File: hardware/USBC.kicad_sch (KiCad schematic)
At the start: 16 parts, among them J20 USB_C_Receptacle_USB2.0_16P, U11 CDSOT236-0504C, U33 USBLC6-2P6, U8 CP2102N-A02-GQFN20

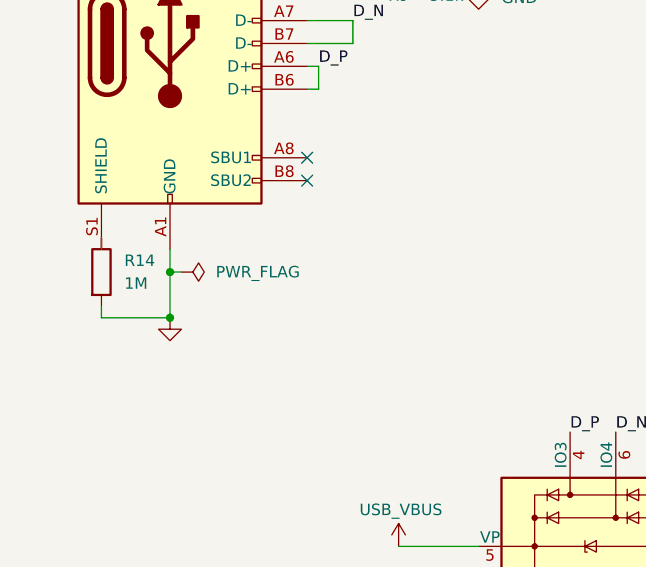
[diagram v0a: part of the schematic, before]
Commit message: passing ERC w/ exclusions
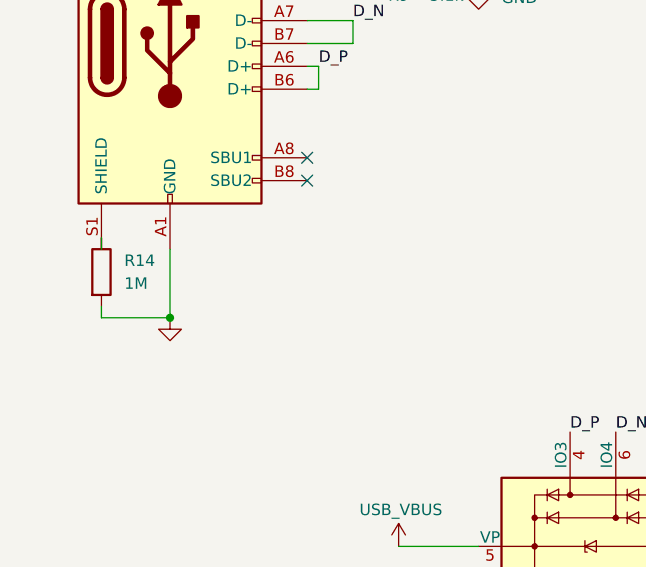
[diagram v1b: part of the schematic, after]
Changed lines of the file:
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@@
-	)
-	(junction
-		(at 55.88 105.41)
-		(diameter 0)
-		(color 0 0 0 0)
 	)
 	(junction
@@
 	(wire
 		(pts
-			(xy 55.88 110.49) (xy 55.88 105.41)
-		)
-		(stroke
-			(width 0)
-			(type default)
-		)
-	)
-	(wire
-		(pts
 			(xy 72.39 82.55) (xy 72.39 85.09)
 		)
@@
 	(wire
 		(pts
-			(xy 55.88 105.41) (xy 55.88 102.87)
+			(xy 55.88 102.87) (xy 55.88 110.49)
 		)
 		(stroke
@@
 		(pts
 			(xy 246.38 100.33) (xy 250.19 100.33)
-		)
-		(stroke
-			(width 0)
-			(type default)
-		)
-	)
-	(wire
-		(pts
-			(xy 55.88 105.41) (xy 57.15 105.41)
 		)
 		(stroke
@@
 					(unit 1)
 				)
-			)
-		)
-	)
-	(symbol
-		(lib_id "power:PWR_FLAG")
-		(at 57.15 105.41 270)
-		(unit 1)
-		(exclude_from_sim no)
-		(in_bom yes)
-		(on_board yes)
-		(dnp no)
-		(fields_autoplaced yes)
-		(property "Reference" "#FLG0108"
-			(at 59.055 105.41 0)
-			(effects
-				(font
-					(size 1.27 1.27)
-				)
-				(hide yes)
-			)
-		)
-		(property "Value" "PWR_FLAG"
-			(at 60.96 105.4099 90)
-			(effects
-				(font
-					(size 1.27 1.27)
-				)
-				(justify left)
-			)
-		)
-		(property "Footprint" ""
-			(at 57.15 105.41 0)
-			(effects
-				(font
-					(size 1.27 1.27)
-				)
-				(hide yes)
-			)
-		)
-		(property "Datasheet" "~"
-			(at 57.15 105.41 0)
-			(effects
-				(font
-					(size 1.27 1.27)
-				)
-				(hide yes)
-			)
-		)
-		(property "Description" "Special symbol for telling ERC where power comes from"
-			(at 57.15 105.41 0)
-			(effects
-				(font
-					(size 1.27 1.27)
-				)
-				(hide yes)
-			)
-		)
-		(pin "1"
-		)
-		(instances
-			(project "Senior_Design"
-				(path "/8f5928e8-0fc1-4443-a20f-3bfeb956761e/53a20cc4-87c9-41e2-9c0c-c30bc75df497"
-					(reference "#FLG0108")
-					(unit 1)
-				)

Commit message: updated annotations
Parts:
- renumbered C90 to C601, C14 to C602, D13 to D601, D14 to D602, J20 to J601, R14 to R601, R300 to R602, R9 to R603, R27 to R604, R28 to R605, R24 to R606, R25 to R607, R26 to R608, U11 to U601, U33 to U602, U8 to U603

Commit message: wip
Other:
- moved on the sheet: C601, C602, D601, D602, J601, R601, R602, R603, R604, R605, R606, R607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

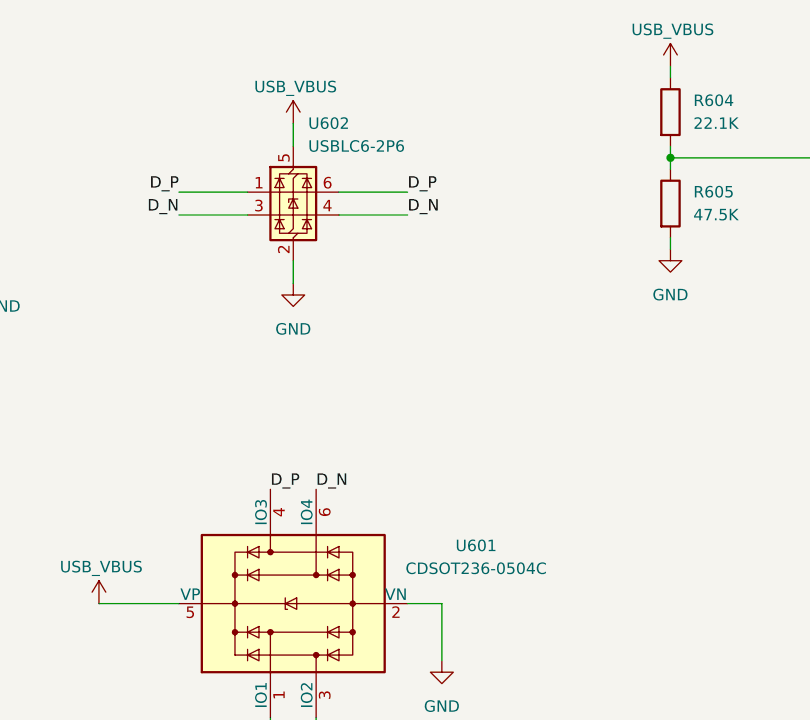
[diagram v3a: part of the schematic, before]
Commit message: added ship fet
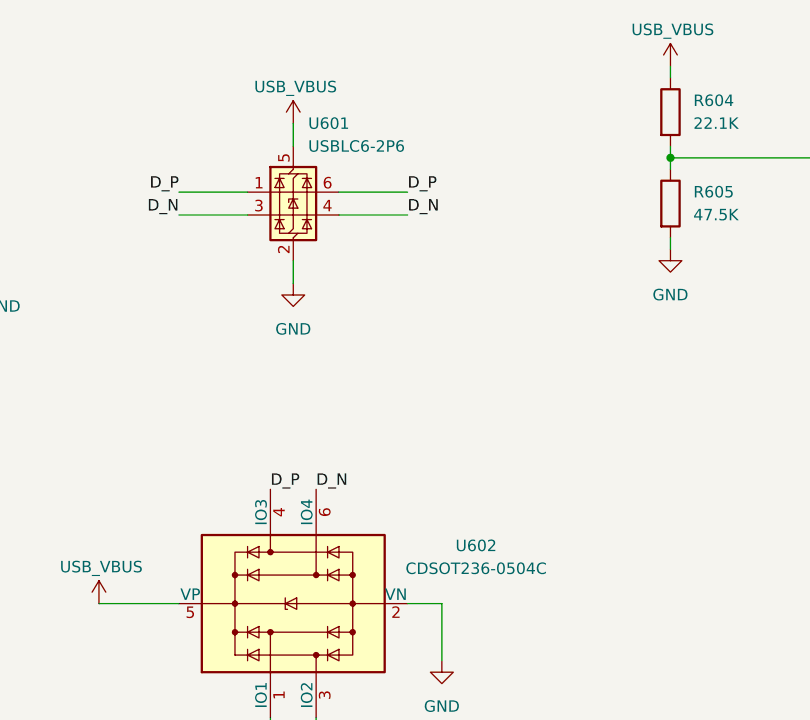
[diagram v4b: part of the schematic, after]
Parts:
- renumbered U602 to U601, U601 to U602
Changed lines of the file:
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@@
+		(dnp no)
+		(fields_autoplaced yes)
+		(property "Reference" "U601"
+			(at 114.6811 57.15 0)
+			(effects
+				(font
+					(size 1.27 1.27)
+				)
+				(justify left)
+			)
+		)
+		(property "Value" "USBLC6-2P6"
+			(at 114.6811 59.69 0)
+			(effects
+				(font
+					(size 1.27 1.27)
+				)
+				(justify left)
+			)
+		)
+		(property "Footprint" "Package_TO_SOT_SMD:SOT-666"
+			(at 114.046 71.501 0)
+			(effects
+				(font
+					(size 1.27 1.27)
+					(italic yes)
+				)
+				(justify left)
+				(hide yes)
+			)
+		)
+		(property "Datasheet" "https://www.st.com/resource/en/datasheet/usblc6-2.pdf"
+			(at 114.046 73.406 0)
+			(effects
+				(font
+					(size 1.27 1.27)
+				)
+				(justify left)
+				(hide yes)
+			)
+		)
+		(property "Description" "Very low capacitance ESD protection diode, 2 data-line, SOT-666"
+			(at 113.03 64.77 0)
+			(effects
+				(font
+					(size 1.27 1.27)
+				)
+				(hide yes)
+			)
+		)
+		(pin "1"
+		)
+		(pin "5"
+		)
+		(pin "3"
+		)
+		(pin "4"
+		)
+		(pin "6"
+		)
+		(pin "2"
+		)
+		(instances
+			(project "Senior_Design"
+				(path "/8f5928e8-0fc1-4443-a20f-3bfeb956761e/53a20cc4-87c9-41e2-9c0c-c30bc75df497"
+					(reference "U601")
+					(unit 1)
+				)
+			)
+		)
+	)
+	(symbol
+		(lib_id "power:GND")
+		(at 76.2 76.2 0)
+		(unit 1)
+		(exclude_from_sim no)
+		(in_bom yes)
+		(on_board yes)
+		(dnp no)
+		(fields_autoplaced yes)
+		(property "Reference" "#PWR0603"
+			(at 76.2 82.55 0)
+			(effects
+				(font
+					(size 1.27 1.27)
+				)
+				(hide yes)
+			)
+		)
+		(property "Value" "GND"
+			(at 78.74 77.4699 0)
+			(effects
+				(font
+					(size 1.27 1.27)
+				)
+				(justify left)
+			)
+		)
+		(property "Footprint" ""
+			(at 76.2 76.2 0)
+			(effects
+				(font
+					(size 1.27 1.27)
+				)
+				(hide yes)
+			)
+		)
+		(property "Datasheet" ""
+			(at 76.2 76.2 0)
+			(effects
+				(font
+					(size 1.27 1.27)
+				)
+				(hide yes)
+			)
+		)
+		(property "Description" "Power symbol creates a global label with name \"GND\" , ground"
+			(at 76.2 76.2 0)
+			(effects
+				(font
+					(size 1.27 1.27)
+				)
+				(hide yes)
+			)
+		)
+		(pin "1"
+		)
+		(instances
+			(project "Senior_Design"
+				(path "/8f5928e8-0fc1-4443-a20f-3bfeb956761e/53a20cc4-87c9-41e2-9c0c-c30bc75df497"
+					(reference "#PWR0603")
+					(unit 1)
+				)
+			)
+		)
+	)
+	(symbol
+		(lib_id "Power_Protection:CDSOT236-0504C")
+		(at 113.03 110.49 90)
+		(unit 1)
+		(exclude_from_sim no)
+		(in_bom yes)
+		(on_board yes)
 		(dnp no)
 		(fields_autoplaced yes)
 		(property "Reference" "U602"
-			(at 114.6811 57.15 0)
-			(effects
-				(font
-					(size 1.27 1.27)
-				)
-				(justify left)
-			)
-		)
-		(property "Value" "USBLC6-2P6"
-			(at 114.6811 59.69 0)
-			(effects
-				(font
-					(size 1.27 1.27)
-				)
-				(justify left)
-			)
-		)
-		(property "Footprint" "Package_TO_SOT_SMD:SOT-666"
-			(at 114.046 71.501 0)
-			(effects
-				(font
-					(size 1.27 1.27)
-					(italic yes)
-				)
-				(justify left)
-				(hide yes)
-			)
-		)
-		(property "Datasheet" "https://www.st.com/resource/en/datasheet/usblc6-2.pdf"
-			(at 114.046 73.406 0)
-			(effects
-				(font
-					(size 1.27 1.27)
-				)
-				(justify left)
-				(hide yes)
-			)
-		)
-		(property "Description" "Very low capacitance ESD protection diode, 2 data-line, SOT-666"
-			(at 113.03 64.77 0)
-			(effects
-				(font
-					(size 1.27 1.27)
-				)
-				(hide yes)
-			)
-		)
-		(pin "1"
-		)
-		(pin "5"
-		)
-		(pin "3"
-		)
-		(pin "4"
-		)
-		(pin "6"
-		)
-		(pin "2"
-		)
-		(instances
-			(project "Senior_Design"
-				(path "/8f5928e8-0fc1-4443-a20f-3bfeb956761e/53a20cc4-87c9-41e2-9c0c-c30bc75df497"
-					(reference "U602")
-					(unit 1)
-				)
-			)
-		)
-	)
-	(symbol
-		(lib_id "power:GND")
-		(at 76.2 76.2 0)
-		(unit 1)
-		(exclude_from_sim no)
-		(in_bom yes)
-		(on_board yes)
-		(dnp no)
-		(fields_autoplaced yes)
-		(property "Reference" "#PWR0604"
-			(at 76.2 82.55 0)
-			(effects
-				(font
-					(size 1.27 1.27)
-				)
-				(hide yes)
-			)
-		)
-		(property "Value" "GND"
-			(at 78.74 77.4699 0)
-			(effects
-				(font
-					(size 1.27 1.27)
-				)
-				(justify left)
-			)
-		)
-		(property "Footprint" ""
-			(at 76.2 76.2 0)
-			(effects
-				(font
-					(size 1.27 1.27)
-				)
-				(hide yes)
-			)
-		)
-		(property "Datasheet" ""
-			(at 76.2 76.2 0)
-			(effects
-				(font
-					(size 1.27 1.27)
-				)
-				(hide yes)
-			)
-		)
-		(property "Description" "Power symbol creates a global label with name \"GND\" , ground"
-			(at 76.2 76.2 0)
-			(effects
-				(font
-					(size 1.27 1.27)
-				)
-				(hide yes)
-			)
-		)
-		(pin "1"
-		)
-		(instances
-			(project "Senior_Design"
-				(path "/8f5928e8-0fc1-4443-a20f-3bfeb956761e/53a20cc4-87c9-41e2-9c0c-c30bc75df497"
-					(reference "#PWR0604")
-					(unit 1)
-				)
-			)
-		)
-	)
-	(symbol
-		(lib_id "Power_Protection:CDSOT236-0504C")
-		(at 113.03 110.49 90)
-		(unit 1)
-		(exclude_from_sim no)
-		(in_bom yes)
-		(on_board yes)
-		(dnp no)
-		(fields_autoplaced yes)
-		(property "Reference" "U601"
 			(at 133.35 104.0698 90)
 			(effects
@@
 			(project ""
 				(path "/8f5928e8-0fc1-4443-a20f-3bfeb956761e/53a20cc4-87c9-41e2-9c0c-c30bc75df497"
-					(reference "U601")
+					(reference "U602")
 					(unit 1)
 				)
@@
 		(on_board yes)
 		(dnp no)
-		(property "Reference" "#PWR0603"
+		(property "Reference" "#PWR0604"
 			(at 91.44 114.3 0)
 			(effects
@@
 			(project "Senior_Design"
 				(path "/8f5928e8-0fc1-4443-a20f-3bfeb956761e/53a20cc4-87c9-41e2-9c0c-c30bc75df497"
-					(reference "#PWR0603")
-					(unit 1)
-				)
+					(reference "#PWR0604")
+					(unit 1)
+				)

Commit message: footprint update
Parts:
- C601, C602: footprint Capacitor_SMD:C_0402_1005Metric -> Capacitor_SMD:C_0805_2012Metric
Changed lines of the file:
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@@
 			)
 		)
-		(property "Footprint" "Capacitor_SMD:C_0402_1005Metric"
+		(property "Footprint" "Capacitor_SMD:C_0805_2012Metric"
 			(at 191.4652 78.74 0)
 			(effects
@@
 			)
 		)
-		(property "Footprint" "Capacitor_SMD:C_0402_1005Metric"
+		(property "Footprint" "Capacitor_SMD:C_0805_2012Metric"
 			(at 180.0352 78.74 0)
 			(effects

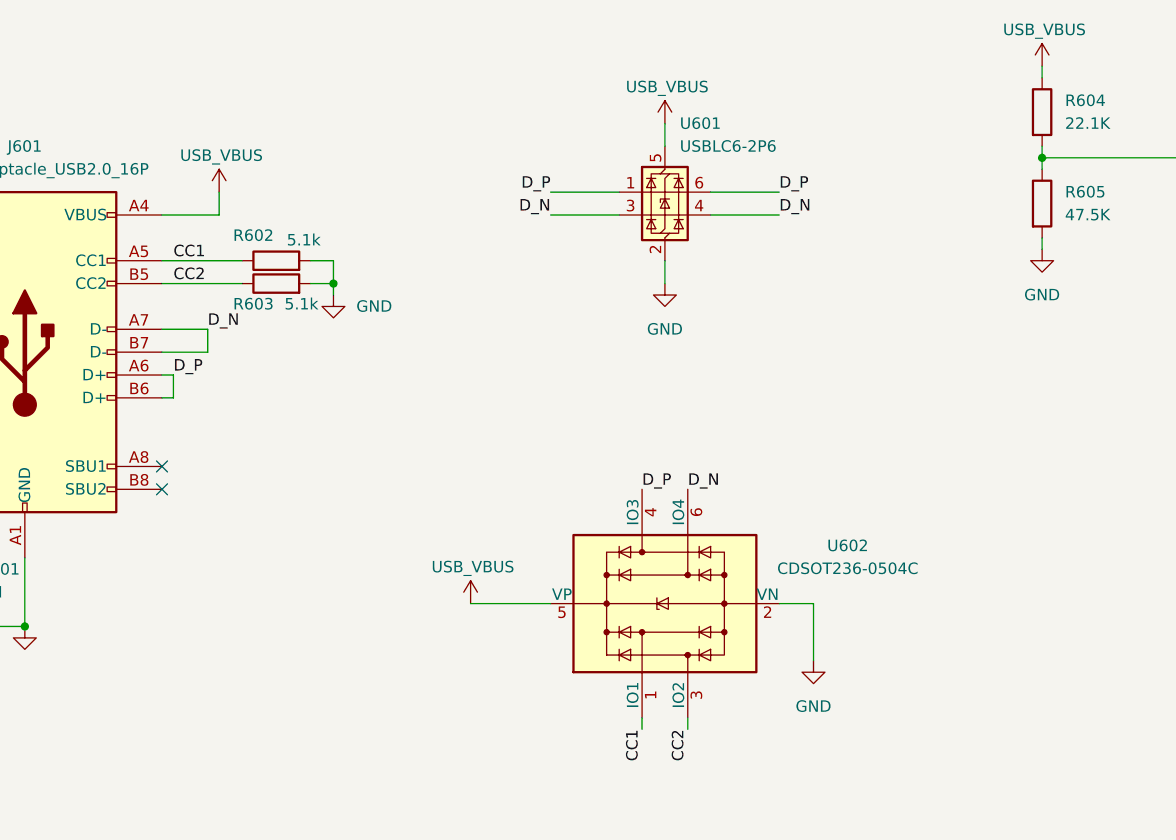
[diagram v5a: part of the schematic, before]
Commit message: updated ESD/Inductor footprints
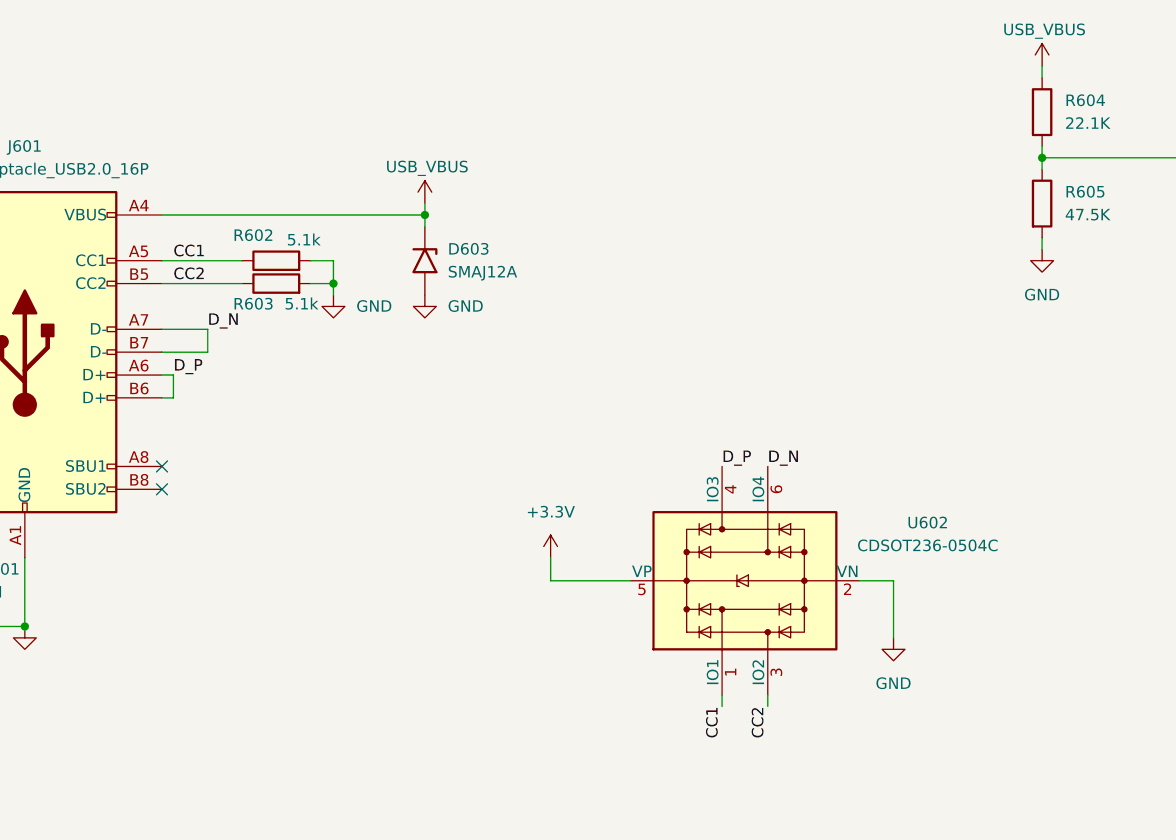
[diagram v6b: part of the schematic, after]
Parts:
- removed U601: USBLC6-2P6, Package_TO_SOT_SMD:SOT-666, symbol Power_Protection:USBLC6-2P6
- added D603: SMAJ12A, Diode_SMD:D_SMA, symbol Diode:SMAJ12A
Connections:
- net +3.3V: now also U602.5 (VP)
- net GND: now also D603.2 (A2)
- net USB_VBUS: now also D603.1 (A1); no longer U602.5 (VP)
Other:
- moved on the sheet: U602

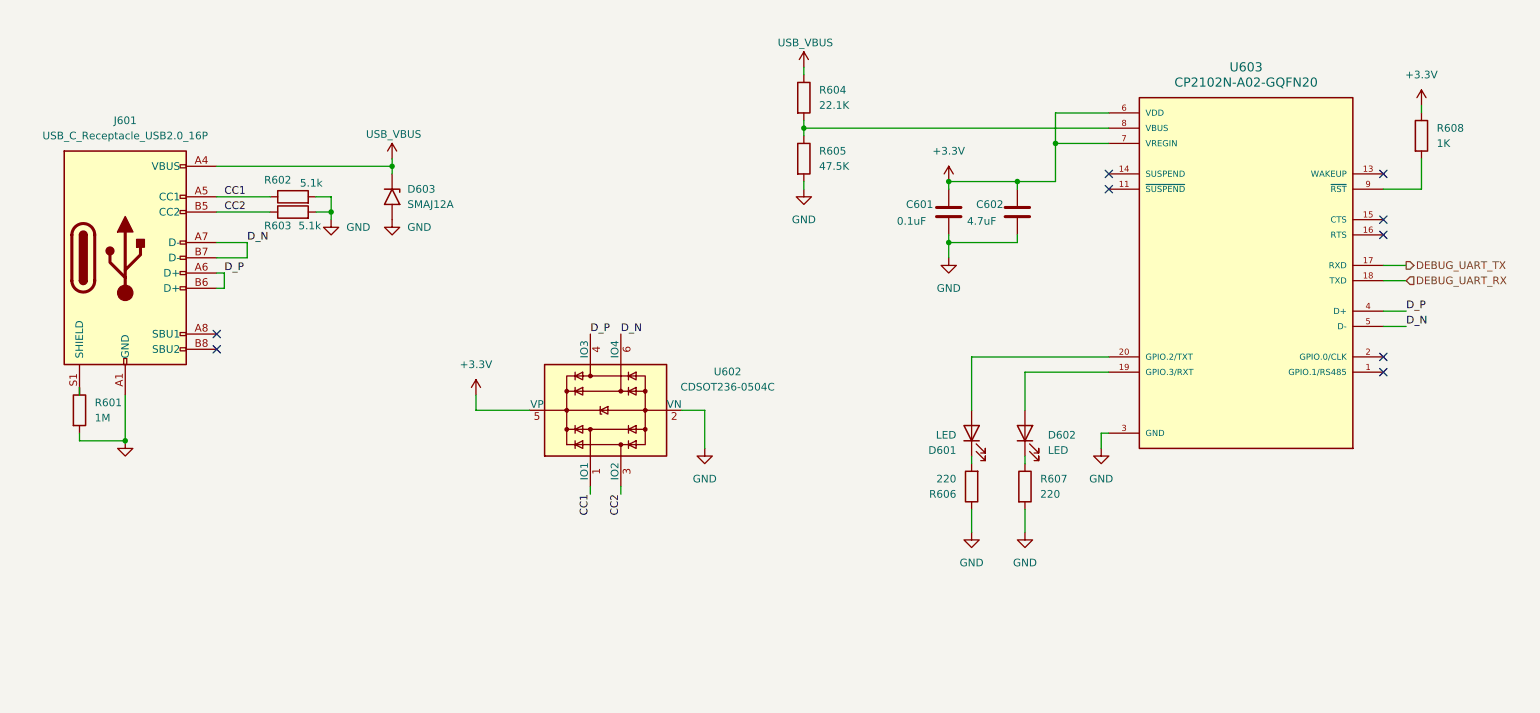
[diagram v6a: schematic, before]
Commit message: updated footprints
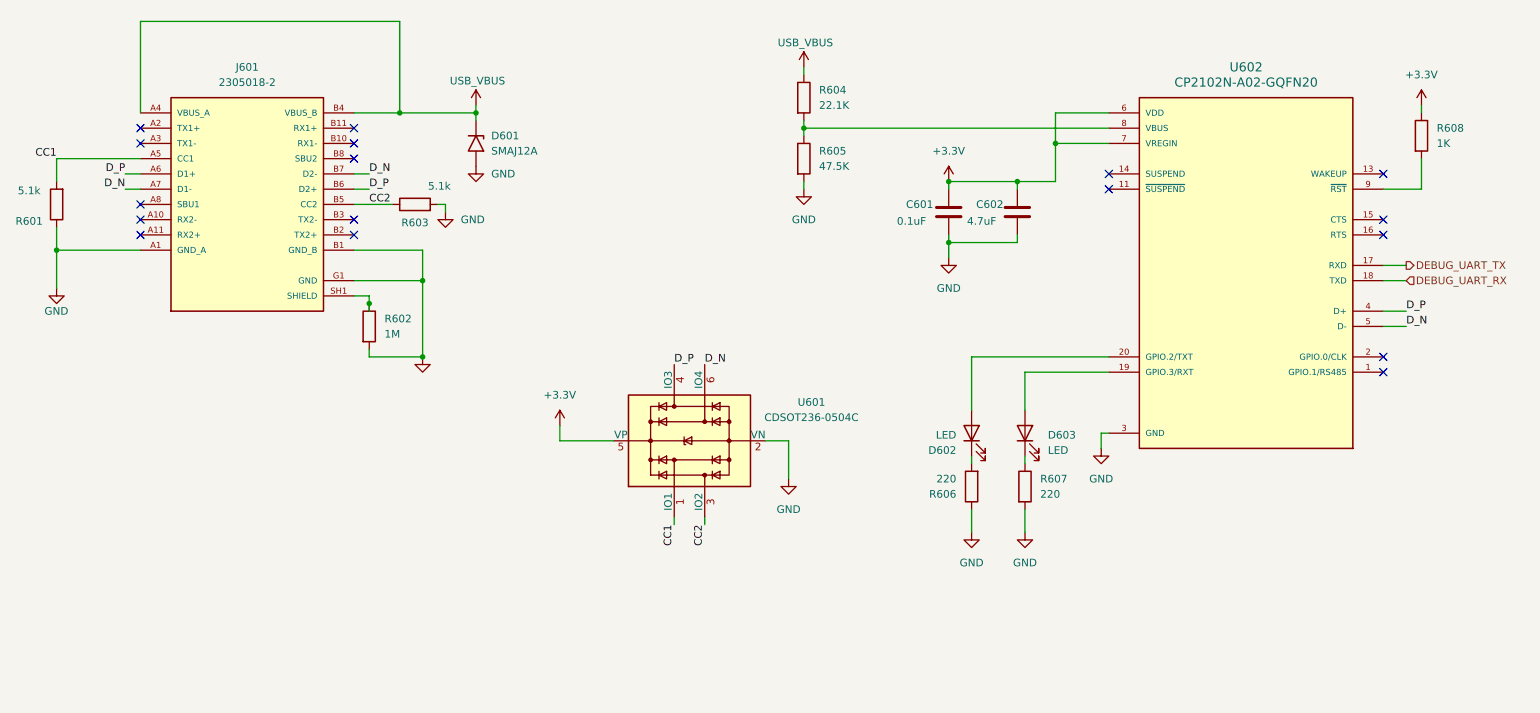
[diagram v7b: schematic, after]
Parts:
- removed D603: SMAJ12A, Diode_SMD:D_SMA, symbol Diode:SMAJ12A
- removed J601: USB_C_Receptacle_USB2.0_16P, Connector_USB:USB_C_Receptacle_HRO_TYPE-C-31-M-12, symbol Connector:USB_C_Receptacle_USB2.0_16P
- added D601: SMAJ12A, Diode_SMD:D_SMA, symbol Diode:SMAJ12A
- added J601: 2305018-2, pyronet_footprints:TE_2305018-2, symbol pyronet_symbols:2305018-2
- R601: value 1M -> 5.1k
- R602: value 5.1k -> 1M
- renumbered D601 to D602, D602 to D603, U602 to U601, U603 to U602
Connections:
- net CC1: now also R601.2, J601.A5 (CC1); no longer R602.1
- net CC2: now also J601.B5 (CC2)
- net D_N: now also J601.A7 (D1-), J601.B7 (D2-)
- net D_P: now also J601.A6 (D1+), J601.B6 (D2+)
- net GND: now also R601.1, D601.2 (A2), J601.A1 (GND_A), J601.A12 (GND_A), J601.B1 (GND_B), J601.B12 (GND_B), J601.G1 (GND), J601.G2 (GND); no longer R601.2
- net USB_VBUS: now also D601.1 (A1), J601.A4 (VBUS_A), J601.A9 (VBUS_A), J601.B4 (VBUS_B), J601.B9 (VBUS_B)
- new net: J601.SH1 (SHIELD), J601.SH2 (SHIELD), J601.SH3 (SHIELD), J601.SH4 (SHIELD), R602.1
- no-connect marks 9 -> 17
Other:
- moved on the sheet: U601
